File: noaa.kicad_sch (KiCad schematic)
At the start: 15 parts, among them J1 USB_C_Receptacle_USB2.0_16P, J2 SMA_F_INT, J3 SMA_F_OUT, U3 GALI-84

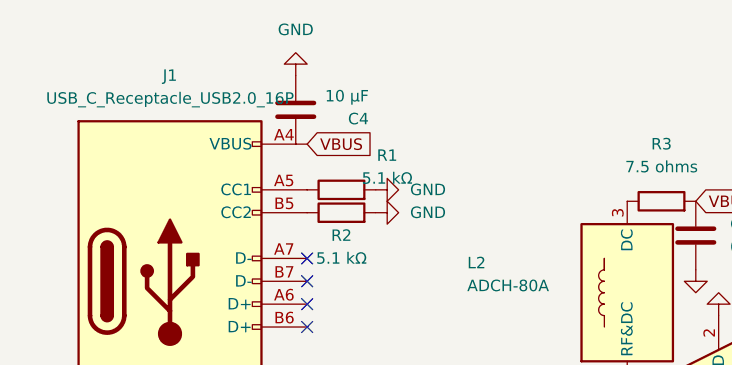
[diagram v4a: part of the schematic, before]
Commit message: Routing should be done
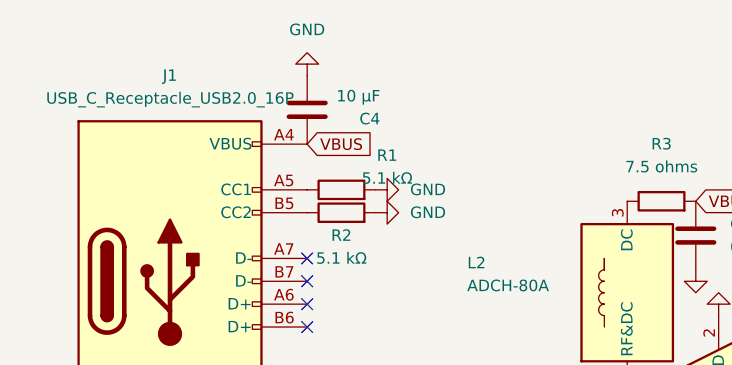
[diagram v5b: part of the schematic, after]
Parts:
- C1, C2, C4, C5, C6: footprint (none) -> Capacitor_SMD:C_0603_1608Metric
- J1: footprint (none) -> Connector_USB:USB_C_Receptacle_GCT_USB4105-xx-A_16P_TopMnt_Horizontal
- J2, J3: footprint (none) -> Connector_Coaxial:SMA_Amphenol_901-143_Horizontal
- L3: footprint (none) -> Inductor_SMD:L_0603_1608Metric
- R1, R2, R3: footprint (none) -> Resistor_SMD:R_0603_1608Metric
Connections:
- net VBUS: now also C4.2
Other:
- moved on the sheet: C4
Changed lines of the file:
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@@
 			)
 		)
-		(property "Footprint" ""
+		(property "Footprint" "Capacitor_SMD:C_0603_1608Metric"
 			(at 104.14 46.0248 0)
 			(effects
@@
 			)
 		)
-		(property "Footprint" ""
+		(property "Footprint" "Capacitor_SMD:C_0603_1608Metric"
 			(at 76.5048 46.99 0)
 			(effects
@@
 			)
 		)
-		(property "Footprint" ""
+		(property "Footprint" "Resistor_SMD:R_0603_1608Metric"
 			(at 82.55 28.448 90)
 			(effects
@@
 			)
 		)
-		(property "Footprint" ""
+		(property "Footprint" "Connector_Coaxial:SMA_Amphenol_901-143_Horizontal"
 			(at 109.22 46.99 0)
 			(effects
@@
 	(symbol
 		(lib_id "power:GND")
-		(at 41.91 12.7 180)
+		(at 43.18 12.7 180)
 		(unit 1)
 		(exclude_from_sim no)
@@
 		(fields_autoplaced yes)
 		(property "Reference" "#PWR07"
-			(at 41.91 6.35 0)
+			(at 43.18 6.35 0)
 			(effects
 				(font
@@
 		)
 		(property "Value" "GND"
-			(at 41.91 7.62 0)
+			(at 43.18 7.62 0)
 			(effects
 				(font
@@
 		)
 		(property "Footprint" ""
-			(at 41.91 12.7 0)
+			(at 43.18 12.7 0)
 			(effects
 				(font
@@
 		)
 		(property "Datasheet" ""
-			(at 41.91 12.7 0)
+			(at 43.18 12.7 0)
 			(effects
 				(font
@@
 		)
 		(property "Description" "Power symbol creates a global label with name \"GND\" , ground"
-			(at 41.91 12.7 0)
+			(at 43.18 12.7 0)
 			(effects
 				(font
@@
 			)
 		)
-		(property "Footprint" ""
+		(property "Footprint" "Resistor_SMD:R_0603_1608Metric"
 			(at 46.99 27.178 90)
 			(effects
@@
 			)
 		)
-		(property "Footprint" ""
+		(property "Footprint" "Connector_USB:USB_C_Receptacle_GCT_USB4105-xx-A_16P_TopMnt_Horizontal"
 			(at 31.75 35.56 0)
 			(effects
@@
 			)
 		)
-		(property "Footprint" ""
+		(property "Footprint" "Inductor_SMD:L_0603_1608Metric"
 			(at 77.47 58.42 0)
 			(effects
@@
 			)
 		)
-		(property "Footprint" ""
+		(property "Footprint" "Capacitor_SMD:C_0603_1608Metric"
 			(at 76.5048 62.23 0)
 			(effects
@@
 			)
 		)
-		(property "Footprint" ""
+		(property "Footprint" "Connector_Coaxial:SMA_Amphenol_901-143_Horizontal"
 			(at 77.47 74.93 0)
 			(effects
@@
 			)
 		)
-		(property "Footprint" ""
+		(property "Footprint" "Capacitor_SMD:C_0603_1608Metric"
 			(at 85.3948 26.67 0)
 			(effects
@@
 	(symbol
 		(lib_id "Device:C")
-		(at 41.91 16.51 0)
+		(at 43.18 16.51 0)
 		(unit 1)
 		(exclude_from_sim no)
@@
 		(dnp no)
 		(property "Reference" "C4"
-			(at 50.038 17.526 0)
+			(at 51.308 17.526 0)
 			(effects
 				(font
@@
 		)
 		(property "Value" "10 μF"
-			(at 50.038 14.986 0)
+			(at 51.308 14.986 0)
 			(effects
 				(font
@@
 			)
 		)
-		(property "Footprint" ""
-			(at 42.8752 20.32 0)
+		(property "Footprint" "Capacitor_SMD:C_0603_1608Metric"
+			(at 44.1452 20.32 0)
 			(effects
 				(font
@@
 		)
 		(property "Datasheet" "~"
-			(at 41.91 16.51 0)
+			(at 43.18 16.51 0)
 			(effects
 				(font
@@
 		)
 		(property "Description" "Unpolarized capacitor"
-			(at 41.91 16.51 0)
+			(at 43.18 16.51 0)
 			(effects
 				(font
@@
 			)
 		)
-		(property "Footprint" ""
+		(property "Footprint" "Resistor_SMD:R_0603_1608Metric"
 			(at 46.99 29.718 90)
 			(effects
